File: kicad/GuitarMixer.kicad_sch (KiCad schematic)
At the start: 35 parts, among them J1 Conn_01x03_Pin, J2 Conn_01x03_Pin, J3 Conn_01x03_Pin, J4 Conn_01x02_Pin, J5 Conn_01x02_Pin, Q1 2N5457, SW1 SW_SPST, U1 TL072, U2 TL072

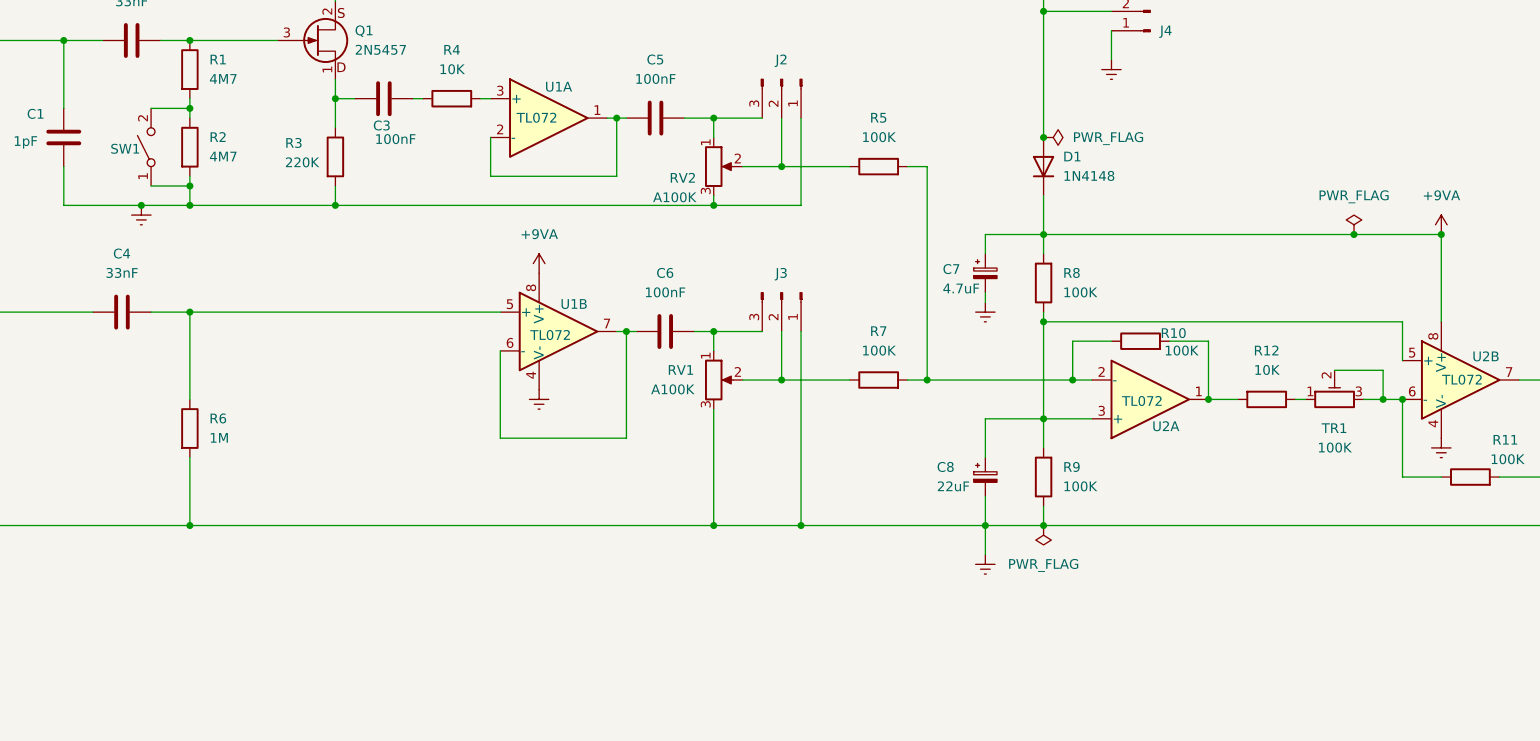
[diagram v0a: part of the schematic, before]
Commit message: Fixed slide switch and changed trimmer to pot connection
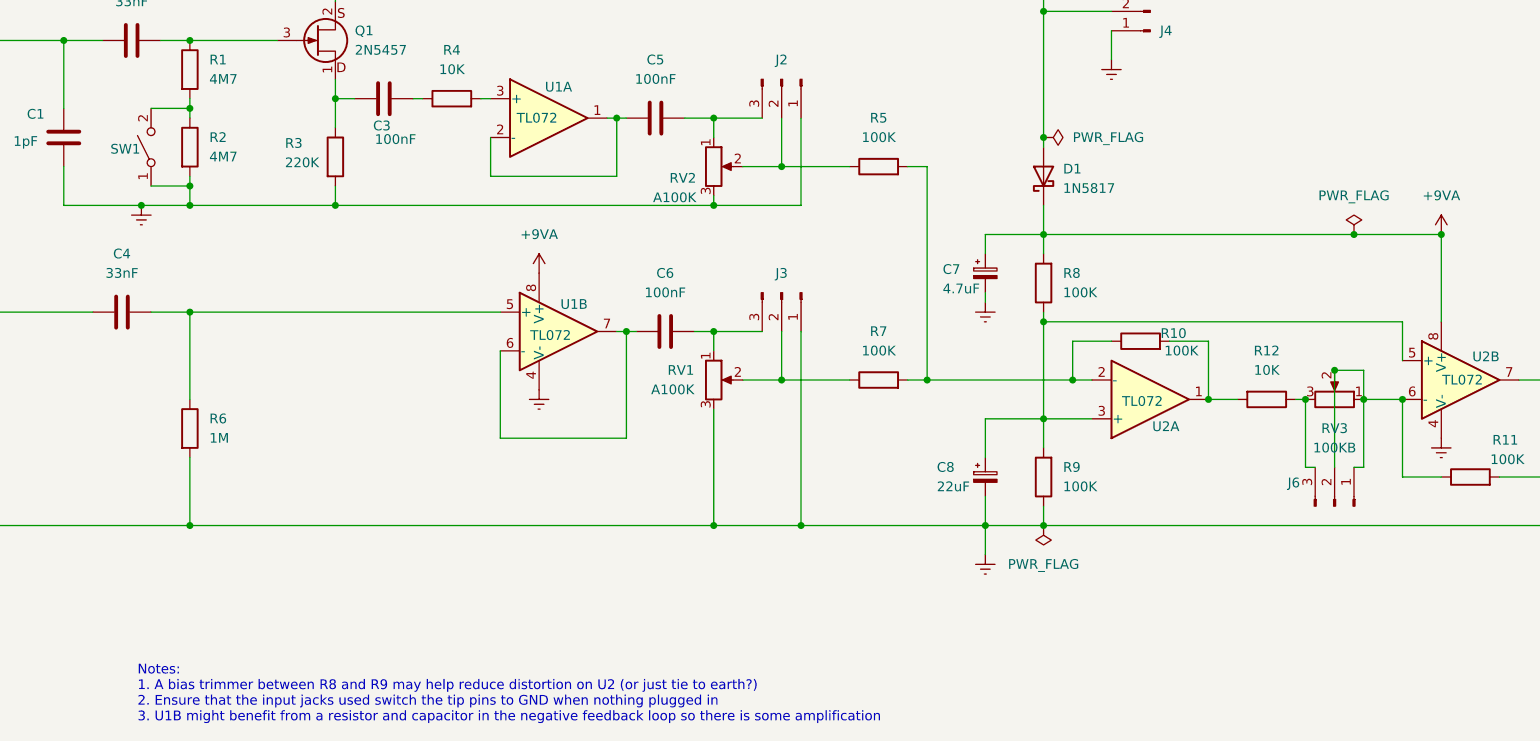
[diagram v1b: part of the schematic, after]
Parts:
- removed D1: 1N4148, Diode_THT:D_DO-35_SOD27_P7.62mm_Horizontal, symbol Diode:1N4148
- removed TR1: 100K, Potentiometer_THT:Potentiometer_Piher_PT-10-V05_Vertical, symbol Device:R_Potentiometer_Trim
- added D1: 1N5817, Diode_THT:D_DO-41_SOD81_P10.16mm_Horizontal, symbol Diode:1N5817
- added J6: Conn_01x03_Pin, Connector_Molex:Molex_KK-254_AE-6410-03A_1x03_P2.54mm_Vertical, symbol Connector:Conn_01x03_Pin
- added RV3: 100KB, symbol Device:R_Potentiometer
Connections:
- net +9V: now also D1.2 (A)
- net +9VA: now also D1.1 (K)
- net at R12.1: now also J6.3 (Pin_3), RV3.3
- net at R11.1, U2.6 (-): now also J6.1 (Pin_1), J6.2 (Pin_2), RV3.1, RV3.2
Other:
- note added: "Notes: 1. A bias trimmer between R8 and R9 may help reduce distortion on U2 (or just tie to earth?) 2. Ensure that the input jacks used switch the tip pins to GND when nothing plugged in 3. U1B might benefit from a resistor and capacitor in the negative feedback loop so there is some amplification"

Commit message: Moved stuff around for separate earth
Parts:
- added JP1: Jumper_2_Open, symbol Jumper:Jumper_2_Open
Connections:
- net Earth: now also JP1.1 (A); no longer C7.2, C8.2, J4.1 (Pin_1), R9.1, U1.4 (V-), U2.4 (V-)
- net +4V: now reaches C8.1, R8.1, R9.2, U2.3 (+), U2.5 (+)
- net +4V: now also JP1.2 (B)
- new net GND: C7.2, C8.2, J4.1 (Pin_1), R9.1, U1.4 (V-), U2.4 (V-)
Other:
- note added: "Acoustic Electric Ground"
- note added: "Signal Ground"
- moved on the sheet: C7, C8, D1, J4, R8, R9

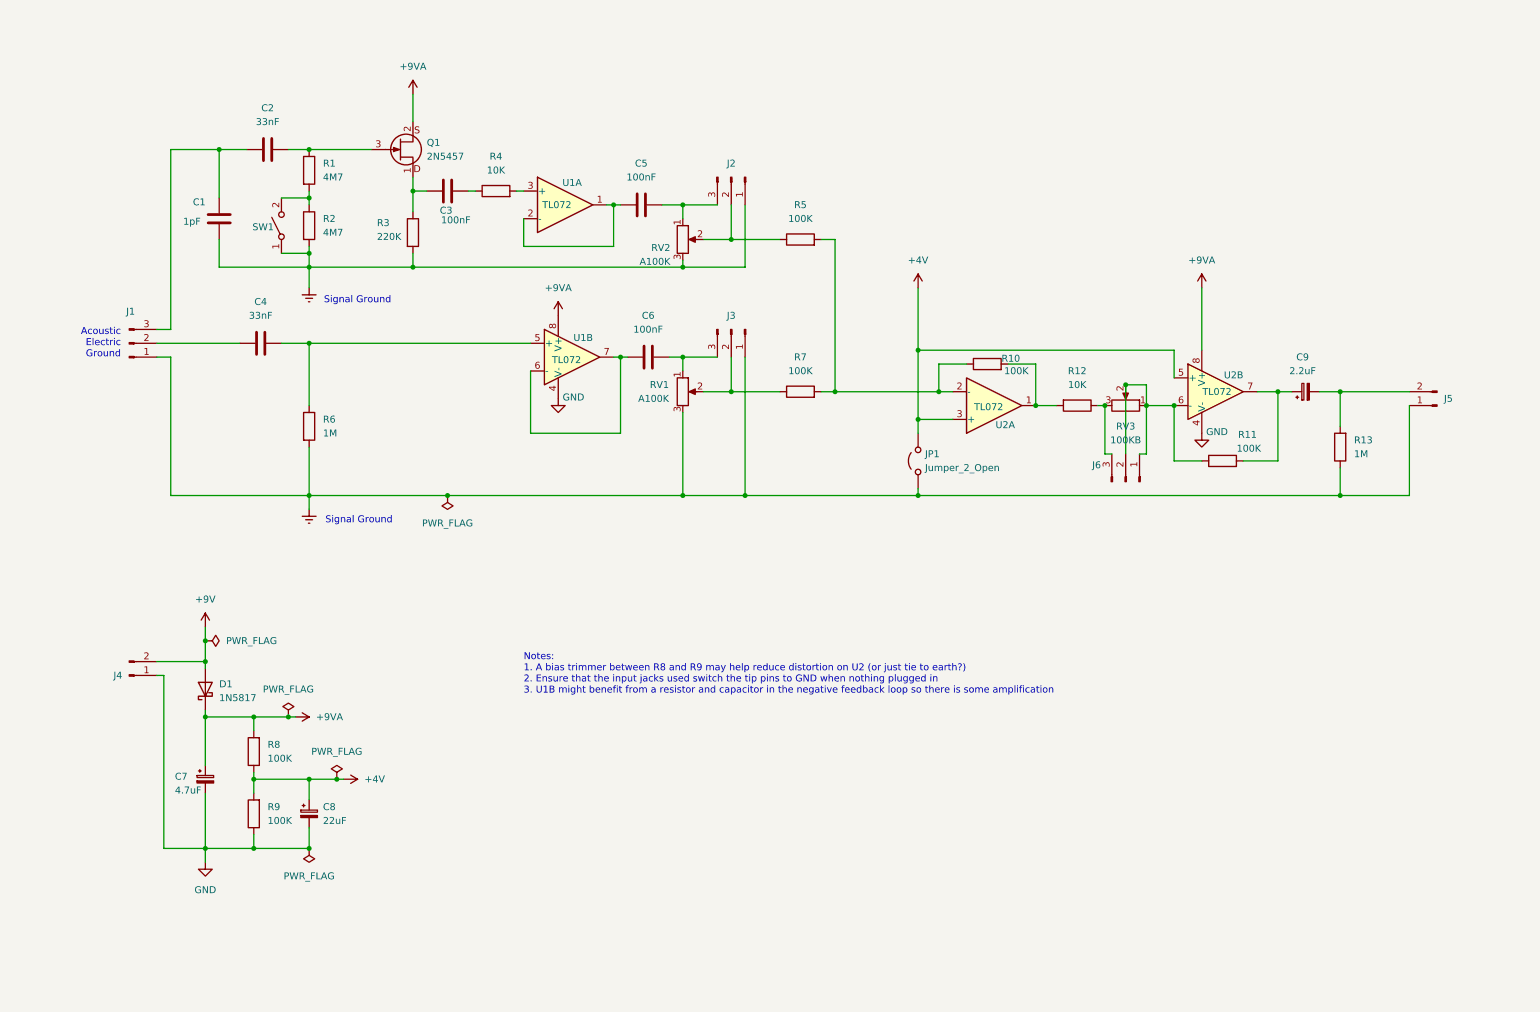
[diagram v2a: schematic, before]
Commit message: Finished test board with lots of options for playing with values
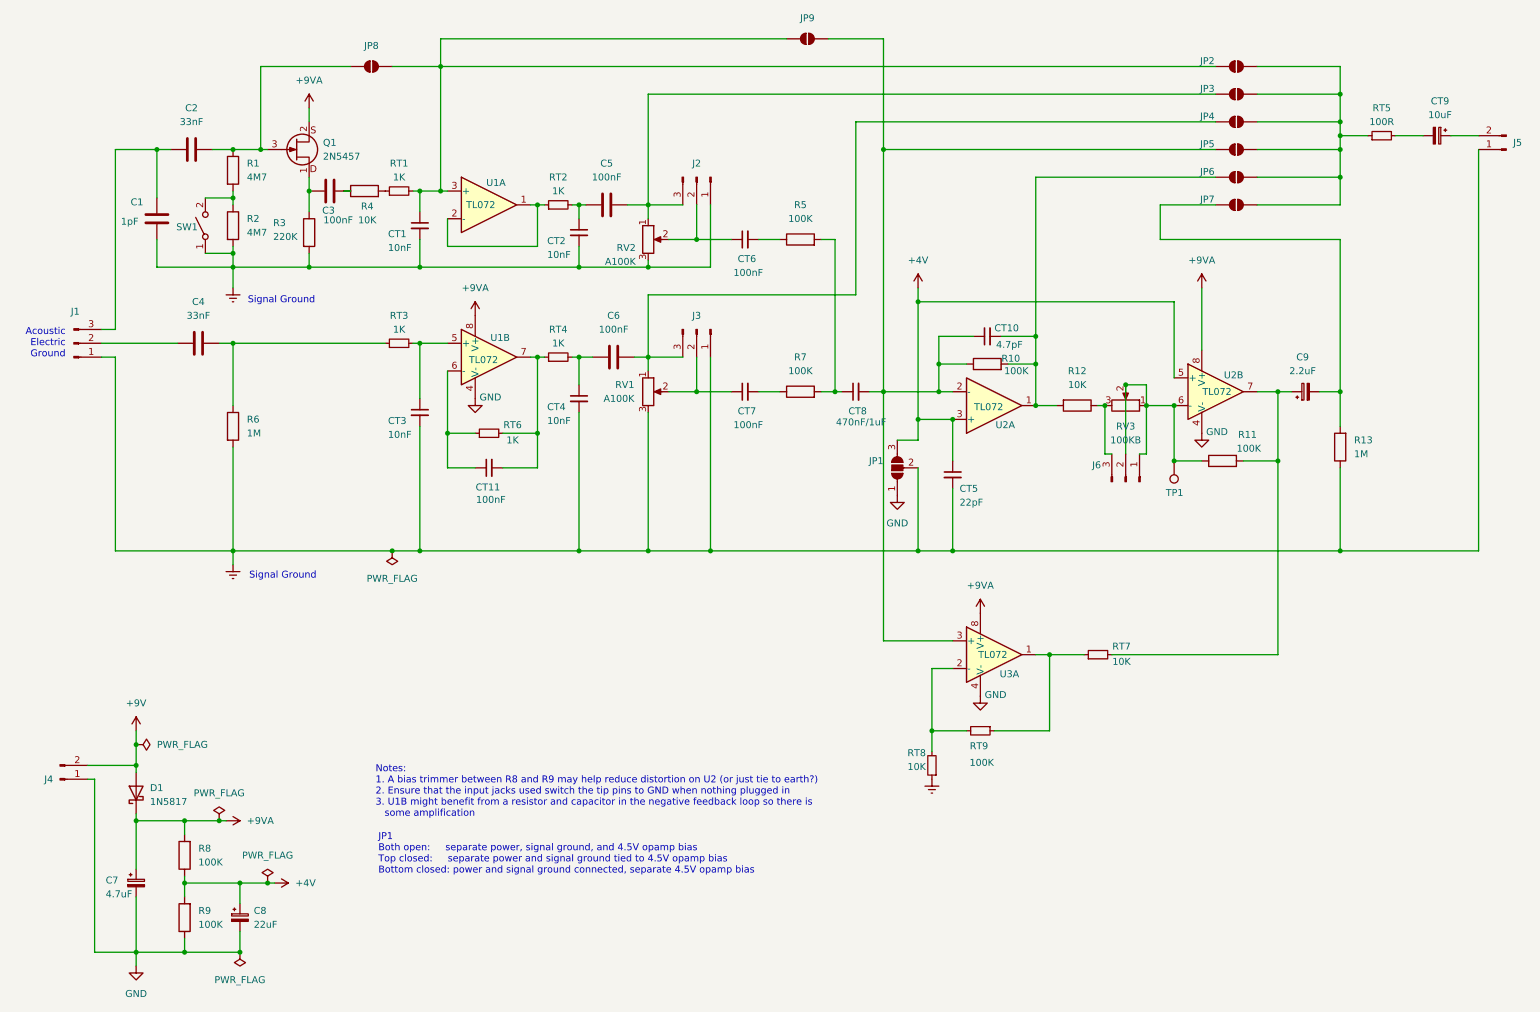
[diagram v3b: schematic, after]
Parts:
- removed JP1: Jumper_2_Open, symbol Jumper:Jumper_2_Open
- added CT1, CT2, CT3, CT4: 10nF, Capacitor_THT:C_Rect_L7.0mm_W3.5mm_P5.00mm, symbol Device:C_Small
- added CT10: 4.7pF, Capacitor_THT:C_Disc_D4.7mm_W2.5mm_P5.00mm, symbol Device:C_Small
- added CT11, CT6, CT7: 100nF, Capacitor_THT:C_Rect_L7.0mm_W3.5mm_P5.00mm, symbol Device:C_Small
- added CT5: 22pF, Capacitor_THT:C_Disc_D4.7mm_W2.5mm_P5.00mm, symbol Device:C_Small
- added CT8: 470nF/1uF, Capacitor_THT:C_Rect_L7.0mm_W3.5mm_P5.00mm, symbol Device:C_Small
- added CT9: 10uF, Capacitor_THT:C_Rect_L7.0mm_W3.5mm_P5.00mm, symbol Device:C_Polarized_Small
- added JP1: SolderJumper_3_Open, Jumper:SolderJumper-3_P1.3mm_Open_Pad1.0x1.5mm, symbol Jumper:SolderJumper_3_Open
- added JP2, JP3, JP4, JP5, JP6, JP7, JP8, JP9: SolderJumper_2_Open, Jumper:SolderJumper-2_P1.3mm_Open_Pad1.0x1.5mm, symbol Jumper:SolderJumper_2_Open
- added RT1, RT2, RT3, RT4, RT6: 1K, Resistor_THT:R_Axial_DIN0207_L6.3mm_D2.5mm_P10.16mm_Horizontal, symbol Device:R_Small
- added RT5: 100R, Resistor_THT:R_Axial_DIN0207_L6.3mm_D2.5mm_P10.16mm_Horizontal, symbol Device:R_Small
- added RT7, RT8: 10K, Resistor_THT:R_Axial_DIN0207_L6.3mm_D2.5mm_P10.16mm_Horizontal, symbol Device:R_Small
- added RT9: 100K, Resistor_THT:R_Axial_DIN0207_L6.3mm_D2.5mm_P10.16mm_Horizontal, symbol Device:R_Small
- added TP1: TestPoint, TestPoint:TestPoint_Pad_2.0x2.0mm, symbol Connector:TestPoint
- added U3: TL072, Package_DIP:DIP-8_W7.62mm, symbol Amplifier_Operational:TL072
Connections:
- net +4V: now also CT5.1, JP1.3 (B)
- net +9VA: now also U3.8 (V+)
- net Earth: now also CT1.2, CT2.2, CT3.2, CT4.2, CT5.2, JP1.2 (C), RT8.1
- net GND: now also JP1.1 (A), U3.4 (V-)
- net at R10.2, R12.2, U2.1: now also CT10.2, JP6.1 (A)
- net at R10.1, U2.2 (-): now also CT10.1, CT8.2, JP5.1 (A), JP9.2 (B), U3.3 (+); no longer R5.2, R7.2
- net at C4.2, R6.1: now also RT3.1; no longer U1.5 (+)
- net at R4.2: now also RT1.1; no longer U1.3 (+)
- net at J6.1 (Pin_1), J6.2 (Pin_2), R11.1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: now also TP1.1
- net at C9.1, R11.2, U2.7: now also RT7.2
- net at C9.2, R13.2: now also JP7.1 (A); no longer J5.2 (Pin_2)
- net at U1.1, U1.2 (-): now also RT2.1; no longer C5.1
- net at C5.2, J2.3 (Pin_3), RV2.1: now also JP3.1 (A)
- net at J3.2 (Pin_2), RV1.2: now also CT7.1; no longer R7.1
- net at J2.2 (Pin_2), RV2.2: now also CT6.1; no longer R5.1
- net at C6.2, J3.3 (Pin_3), RV1.1: now also JP4.1 (A)
- net at C2.2, Q1.3 (G), R1.1: now also JP8.1 (A)
- new net: CT11.2, RT4.1, RT6.2, U1.7
- new net: C6.1, CT4.1, RT4.2
- new net: CT9.1, J5.2 (Pin_2)
- new net: CT9.2, RT5.2
- new net: CT11.1, RT6.1, U1.6 (-)
- new net: CT6.2, R5.1
- new net: CT8.1, R5.2, R7.2
- new net: JP2.2 (B), JP3.2 (B), JP4.2 (B), JP5.2 (B), JP6.2 (B), JP7.2 (B), RT5.1
- new net: CT1.1, JP2.1 (A), JP8.2 (B), JP9.1 (A), RT1.2, U1.3 (+)
- new net: C5.1, CT2.1, RT2.2
- new net: CT7.2, R7.1
- new net: RT8.2, RT9.2, U3.2 (-)
- new net: CT3.1, RT3.2, U1.5 (+)
- new net: RT7.1, RT9.1, U3.1
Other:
- note added: "JP1 Both open: separate power, signal ground, and 4.5V opamp bias Top closed: separate power and signal ground tied to 4.5V opamp bias Bottom closed: power and signal ground connected, separate 4.5V opamp bias"
- moved on the sheet: C1, C2, C3, C4, C5, C6, C7, C8, D1, J1, J2, J3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
